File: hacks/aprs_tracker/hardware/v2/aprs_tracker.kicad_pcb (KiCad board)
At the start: 2 copper layers, 91.8 x 108.2 mm, 43 parts, among them J1 SMA, P1 POWER, P2 TEMPERATURE, P3 GPS, Q1 2N7002, Q2 2N7002, U1 DRA818V

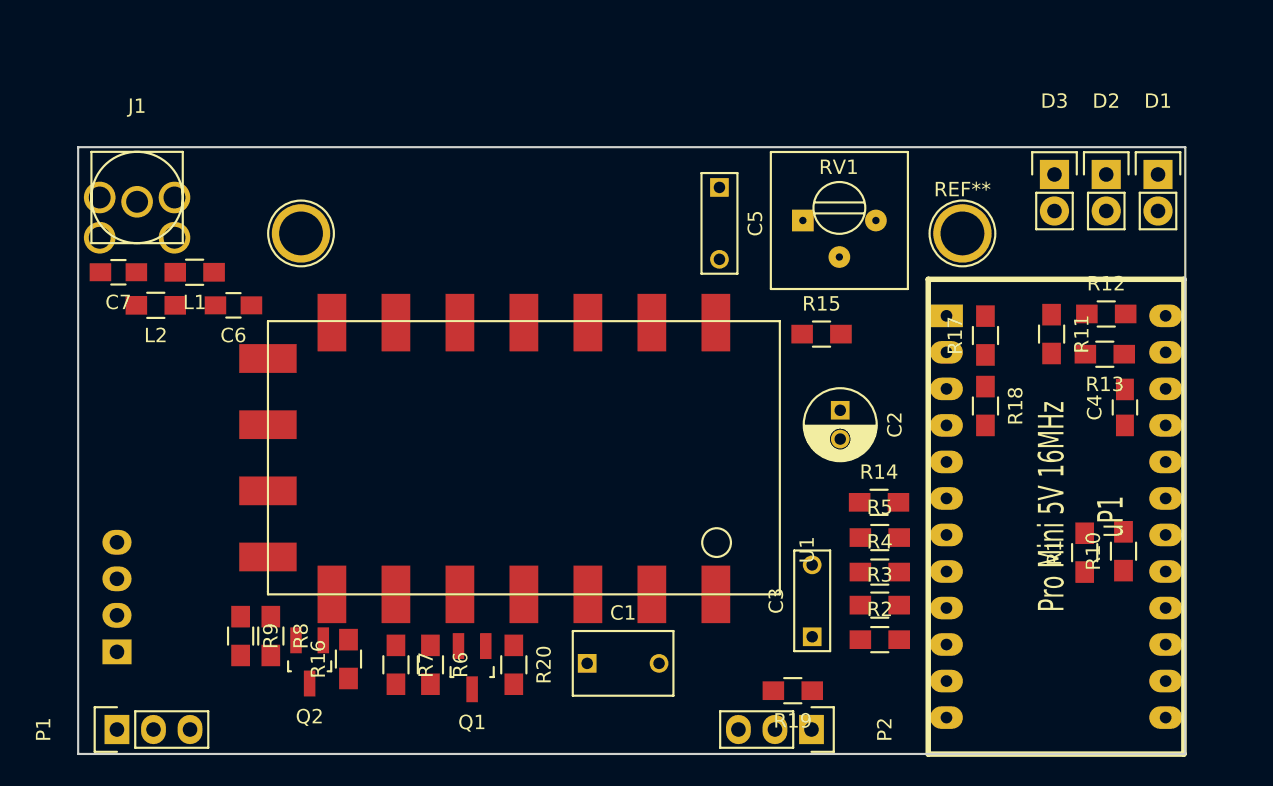
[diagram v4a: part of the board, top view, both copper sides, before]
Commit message: placement and wiring ready and tested
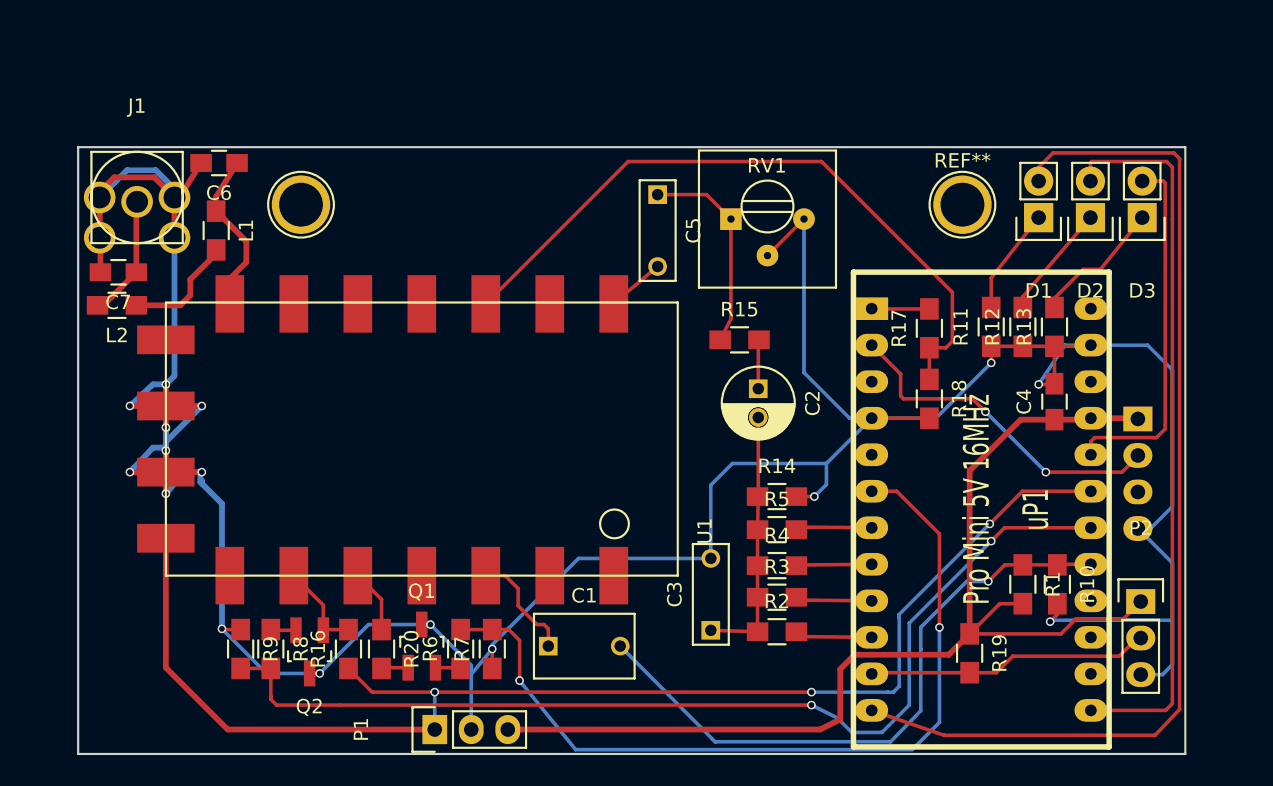
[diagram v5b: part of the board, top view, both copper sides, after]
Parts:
- moved P3 72.8 mm to (167.1, 112.5), turned to 180 degrees
- moved P2 24.6 mm to (167.3, 125.2), turned to 0 degrees
- moved P1 22.1 mm to (118.2, 134.1)
- moved R19 12.6 mm to (155.4, 128.8), turned to 270 degrees
- moved C6 9.95 mm to (103.2, 94.7)
- moved R20 9.27 mm to (114.5, 128.5)
- moved D1 8.83 mm to (160.2, 98.5), turned to 180 degrees
- moved U1 7.22 mm to (135.1, 123.4)
- moved R2 7.17 mm to (142.0, 127.3)
- moved R3 7.17 mm to (142.0, 124.9)
- moved R5 7.17 mm to (142.0, 120.2)
- moved R4 7.16 mm to (142.0, 122.7)
- moved R14 7.11 mm to (142.0, 117.9)
- moved C3 7.06 mm to (137.4, 127.2)
- moved D3 6.80 mm to (167.4, 98.5), turned to 180 degrees
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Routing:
- net GND: track 0.00 -> 243.1 mm, vias 0 -> 16
- net /V_BATT: track 0.00 -> 93.3 mm, vias 0 -> 3
- net +5V: track 0.00 -> 80.0 mm
- net /D9: track 0.00 -> 72.1 mm
- net /RADIO_PD_CONTROL: track 0.00 -> 71.3 mm, vias 0 -> 2
- net /PTT_CONTROL: track 0.00 -> 58.5 mm, vias 0 -> 2
- net /D10: track 0.00 -> 50.3 mm
- net /RADIO_TX: track 0.00 -> 48.0 mm
- net /AUDIO_IN: track 0.00 -> 44.0 mm, vias 0 -> 1
- net /STATUS_LED: track 0.00 -> 25.2 mm
- net /GPS_RX: track 0.00 -> 23.6 mm, vias 0 -> 2
- net /TEMP_DATA: track 0.00 -> 19.8 mm
- net Net-(C2-Pad2): track 0.00 -> 18.8 mm
- net /MIC_LEVEL_OUT: track 0.00 -> 14.5 mm
- net Net-(C6-Pad1): track 0.00 -> 13.9 mm
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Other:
- net class Thick added: clearance 0.2, trace_width 0.4, via_dia 0.6, via_drill 0.4

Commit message: board iter 1 ready
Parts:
- moved R4 0.10 mm to (142.0, 122.6)
- moved R5 0.10 mm to (142.0, 120.3)
- renumbered P1 to Power, D2 to RX, D3 to STAT., D1 to TX, P2 to Temp
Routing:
- net GND: track 243.1 -> 337.6 mm
- added copper zone on B.Cu, net GND
- added copper zone on F.Cu, net GND
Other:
- board text added: "APRS tracker using DRA818V VHF 1W radio and Arduino Pro Mini 5V 16MHz. By @mik4el4ndersson 2016 V01."
- board text added: "GND DATA +5V"
- board text added: "LEDs"
- board text added: "V_batt GND +5V"

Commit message: ordered pcbs
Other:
- board size 91.8 x 108.2 mm -> 77 x 42.2 mm
- net class Default: clearance 0.2 -> 0.0762
- net class Thick: clearance 0.2 -> 0.0762
- rule pad_to_mask_clearance: 0.2 -> 0.0762
- rule trace_clearance: 0.2 -> 0.0762
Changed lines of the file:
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@@
     (links 80)
     (no_connects 0)
-    (area 92.705953 27.524999 185.275001 136.922619)
+    (area 87.2 89 173.900001 138.400001)
     (thickness 1.6)
-    (drawings 9)
+    (drawings 8)
     (tracks 466)
     (zones 0)
@@
     (last_trace_width 0.4)
     (user_trace_width 0.4)
-    (trace_clearance 0.2)
+    (trace_clearance 0.0762)
     (zone_clearance 0.3)
     (zone_45_only no)
@@
     (pad_size 1.524 1.524)
     (pad_drill 0.762)
-    (pad_to_mask_clearance 0.2)
+    (pad_to_mask_clearance 0.0762)
     (aux_axis_origin 0 0)
     (grid_origin 93.4 93.6)
     (visible_elements FFFFFF7F)
     (pcbplotparams
-      (layerselection 0x00030_80000001)
-      (usegerberextensions false)
+      (layerselection 0x010f0_80000001)
+      (usegerberextensions true)
       (excludeedgelayer true)
       (linewidth 0.100000)
@@
       (outputformat 1)
       (mirror false)
-      (drillshape 1)
+      (drillshape 0)
       (scaleselection 1)
-      (outputdirectory ""))
+      (outputdirectory export/))
   )
   (net 0 "")
@@
   (net 33 "Net-(R17-Pad2)")
   (net_class Default "This is the default net class."
-    (clearance 0.2)
+    (clearance 0.0762)
     (trace_width 0.25)
     (via_dia 0.6)
@@
   )
   (net_class Thick ""
-    (clearance 0.2)
+    (clearance 0.0762)
     (trace_width 0.4)
     (via_dia 0.6)
@@
     (pad 1 thru_hole circle (at 0 0) (size 4.064 4.064) (drill 3.048) (layers *.Cu *.Mask F.SilkS))
   )
+  (gr_text "GND DATA +5V" (at 169.7 127.7 90) (layer F.SilkS)
+    (effects (font (size 0.6 0.6) (thickness 0.06)))
+  )
   (gr_text "APRS tracker using \nDRA818V VHF 1W radio and \nArduino Pro Mini 5V 16MHz. \nBy @mik4el4ndersson 2016 V01." (at 131.4 105.5) (layer B.SilkS)
     (effects (font (size 1.5 1.5) (thickness 0.3)) (justify left mirror))
   )
-  (gr_text "GND DATA +5V" (at 169.7 127.7 90) (layer F.SilkS)
-    (effects (font (size 0.6 0.6) (thickness 0.06)))
-  )
   (gr_text LEDs (at 156.7 94.5) (layer F.SilkS)
     (effects (font (size 1 1) (thickness 0.1)))
@@
     (effects (font (size 0.6 0.6) (thickness 0.06)))
   )
-  (gr_line (start 185.2 27.9) (end 185.2 27.6) (angle 90) (layer Edge.Cuts) (width 0.15))
   (gr_line (start 93.4 93.6) (end 170.4 93.6) (angle 90) (layer Edge.Cuts) (width 0.15))
   (gr_line (start 170.4 93.6) (end 170.4 135.8) (angle 90) (layer Edge.Cuts) (width 0.15))
@@
   (segment (start 148.61 104.85) (end 148.59 104.83) (width 0.25) (layer F.Cu) (net 33))
   (segment (start 152.58 104.83) (end 152.6 104.85) (width 0.25) (layer F.Cu) (net 33) (status 30))
-  (zone (net 5) (net_name GND) (layer B.Cu) (hatch edge 0.508)
-    (connect_pads (clearance 0.508))
-    (min_thickness 0.254)
-    (fill yes (arc_segments 16) (thermal_gap 0.508) (thermal_bridge_width 0.508))
-    (polygon
-      (pts
-        (xy 90.2 90.4) (xy 89.8 138.4) (xy 173.9 138.4) (xy 173.7 90.4)
-      )
-    )
-  )
   (zone (net 5) (net_name GND) (layer F.Cu) (hatch edge 0.508)
     (connect_pads (clearance 0.3))
@@
       )
     )
+  )
+  (zone (net 5) (net_name GND) (layer B.Cu) (hatch edge 0.508)
+    (connect_pads (clearance 0.508))
+    (min_thickness 0.254)
+    (fill yes (arc_segments 16) (thermal_gap 0.508) (thermal_bridge_width 0.508))
+    (polygon
+      (pts
+        (xy 90.2 90.4) (xy 89.8 138.4) (xy 173.9 138.4) (xy 173.7 90.4)
+      )
+    )
